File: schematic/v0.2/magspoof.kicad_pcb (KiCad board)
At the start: 2 copper layers, 29.2 x 39.4 mm, 23 parts, among them IC1 STM32F042G6U6, IC3 DRV8835DSSR, P1 USB_A, P2 Expansion Port, P3 Ext Clock, P4 Program Port, SW1 Select, SW2 FIRE!, U1 MCP73831-2-OT

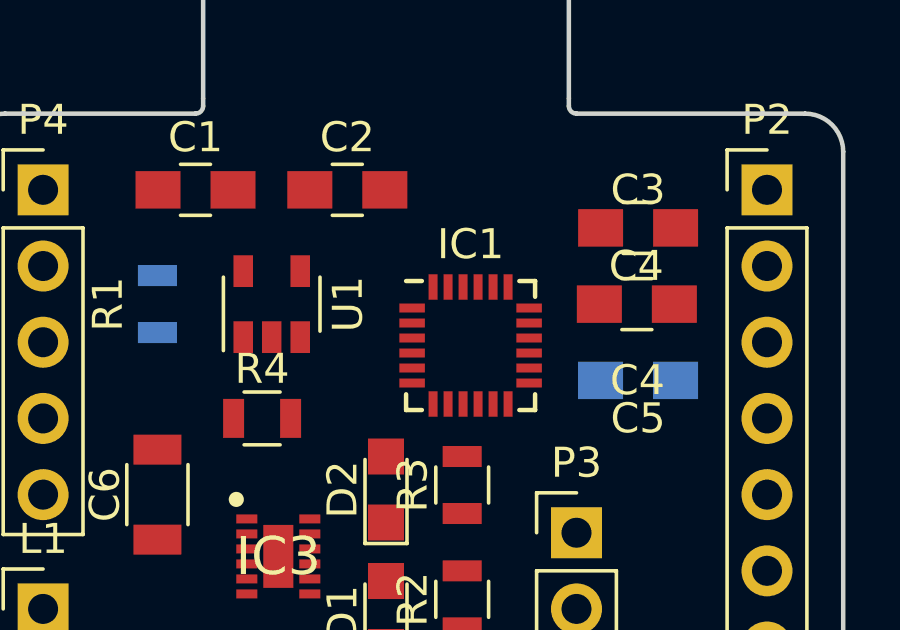
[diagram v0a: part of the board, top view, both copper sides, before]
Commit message: Changed stm32 footprint
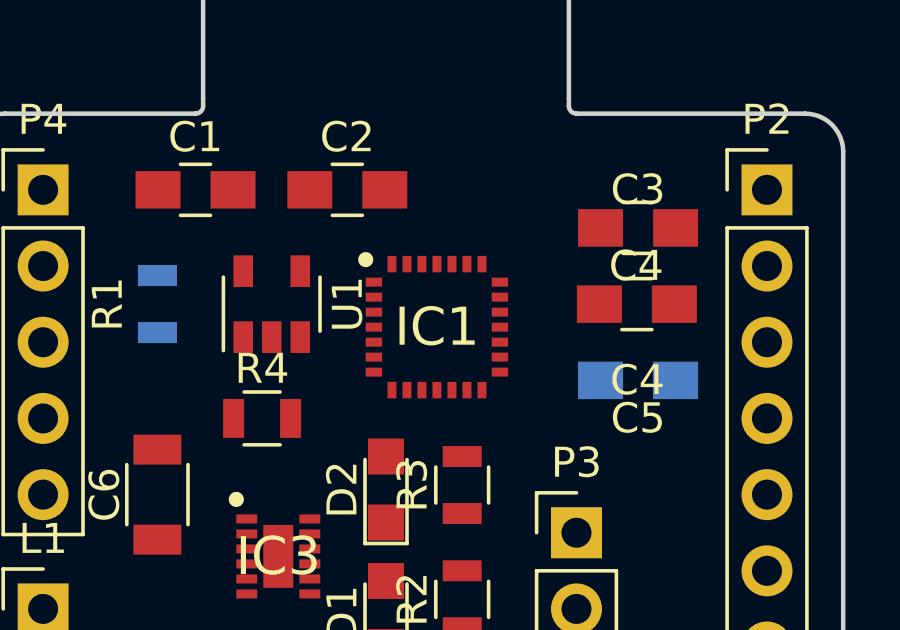
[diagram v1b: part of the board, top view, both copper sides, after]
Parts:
- IC1: footprint Housings_DFN_QFN:QFN-24_4x4mm_Pitch0.5mm -> STM32F042G6U6:QFN50P400X400X60-28N
- moved IC1 1.28 mm to (151.6, 104.9)
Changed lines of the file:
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@@
 (kicad_pcb (version 4) (host pcbnew 4.0.4-stable)
   (general
-    (links 51)
-    (no_connects 51)
-    (area 0 0 0 0)
+    (links 55)
+    (no_connects 55)
+    (area 135.814999 85.014999 165.175001 124.535001)
     (thickness 1.6)
     (drawings 16)
@@
     )
   )
-  (module Housings_DFN_QFN:QFN-24_4x4mm_Pitch0.5mm (layer F.Cu)
-    (at 152.68 105.52)
-    (descr "24-Lead Plastic Quad Flat, No Lead Package (MJ) - 4x4x0.9 mm Body [QFN]; (see Microchip Packaging Specification 00000049BS.pdf)")
-    (tags "QFN 0.5")
-    (attr smd)
-    (fp_text reference IC1 (at 0 -3.375) (layer F.SilkS)
-      (effects (font (size 1 1) (thickness 0.15)))
-    )
-    (fp_text value STM32F042G6U6 (at 0 3.375) (layer F.Fab)
-      (effects (font (size 1 1) (thickness 0.15)))
-    )
-    (fp_line (start -1 -2) (end 2 -2) (layer F.Fab) (width 0.15))
-    (fp_line (start 2 -2) (end 2 2) (layer F.Fab) (width 0.15))
-    (fp_line (start 2 2) (end -2 2) (layer F.Fab) (width 0.15))
-    (fp_line (start -2 2) (end -2 -1) (layer F.Fab) (width 0.15))
-    (fp_line (start -2 -1) (end -1 -2) (layer F.Fab) (width 0.15))
-    (fp_line (start -2.65 -2.65) (end -2.65 2.65) (layer F.CrtYd) (width 0.05))
-    (fp_line (start 2.65 -2.65) (end 2.65 2.65) (layer F.CrtYd) (width 0.05))
-    (fp_line (start -2.65 -2.65) (end 2.65 -2.65) (layer F.CrtYd) (width 0.05))
-    (fp_line (start -2.65 2.65) (end 2.65 2.65) (layer F.CrtYd) (width 0.05))
-    (fp_line (start 2.15 -2.15) (end 2.15 -1.625) (layer F.SilkS) (width 0.15))
-    (fp_line (start -2.15 2.15) (end -2.15 1.625) (layer F.SilkS) (width 0.15))
-    (fp_line (start 2.15 2.15) (end 2.15 1.625) (layer F.SilkS) (width 0.15))
-    (fp_line (start -2.15 -2.15) (end -1.625 -2.15) (layer F.SilkS) (width 0.15))
-    (fp_line (start -2.15 2.15) (end -1.625 2.15) (layer F.SilkS) (width 0.15))
-    (fp_line (start 2.15 2.15) (end 1.625 2.15) (layer F.SilkS) (width 0.15))
-    (fp_line (start 2.15 -2.15) (end 1.625 -2.15) (layer F.SilkS) (width 0.15))
-    (pad 1 smd rect (at -1.95 -1.25) (size 0.85 0.3) (layers F.Cu F.Paste F.Mask)
-      (net 8 "Net-(IC1-Pad1)"))
-    (pad 2 smd rect (at -1.95 -0.75) (size 0.85 0.3) (layers F.Cu F.Paste F.Mask)
-      (net 9 "Net-(IC1-Pad2)"))
-    (pad 3 smd rect (at -1.95 -0.25) (size 0.85 0.3) (layers F.Cu F.Paste F.Mask)
-      (net 10 "Net-(IC1-Pad3)"))
-    (pad 4 smd rect (at -1.95 0.25) (size 0.85 0.3) (layers F.Cu F.Paste F.Mask)
-      (net 11 RESET))
-    (pad 5 smd rect (at -1.95 0.75) (size 0.85 0.3) (layers F.Cu F.Paste F.Mask)
-      (net 12 "Net-(IC1-Pad5)"))
-    (pad 6 smd rect (at -1.95 1.25) (size 0.85 0.3) (layers F.Cu F.Paste F.Mask)
-      (net 13 "Net-(IC1-Pad6)"))
-    (pad 7 smd rect (at -1.25 1.95 90) (size 0.85 0.3) (layers F.Cu F.Paste F.Mask)
-      (net 14 "Net-(IC1-Pad7)"))
-    (pad 8 smd rect (at -0.75 1.95 90) (size 0.85 0.3) (layers F.Cu F.Paste F.Mask)
-      (net 6 LED1))
-    (pad 9 smd rect (at -0.25 1.95 90) (size 0.85 0.3) (layers F.Cu F.Paste F.Mask)
-      (net 15 "Net-(IC1-Pad9)"))
-    (pad 10 smd rect (at 0.25 1.95 90) (size 0.85 0.3) (layers F.Cu F.Paste F.Mask)
-      (net 16 "Net-(IC1-Pad10)"))
-    (pad 11 smd rect (at 0.75 1.95 90) (size 0.85 0.3) (layers F.Cu F.Paste F.Mask)
-      (net 17 SW2))
-    (pad 12 smd rect (at 1.25 1.95 90) (size 0.85 0.3) (layers F.Cu F.Paste F.Mask)
-      (net 18 SW1))
-    (pad 13 smd rect (at 1.95 1.25) (size 0.85 0.3) (layers F.Cu F.Paste F.Mask)
-      (net 4 LED2))
-    (pad 14 smd rect (at 1.95 0.75) (size 0.85 0.3) (layers F.Cu F.Paste F.Mask)
-      (net 19 STATUS_LED))
-    (pad 15 smd rect (at 1.95 0.25) (size 0.85 0.3) (layers F.Cu F.Paste F.Mask)
-      (net 20 "Net-(IC1-Pad15)"))
-    (pad 16 smd rect (at 1.95 -0.25) (size 0.85 0.3) (layers F.Cu F.Paste F.Mask)
-      (net 2 GND))
-    (pad 17 smd rect (at 1.95 -0.75) (size 0.85 0.3) (layers F.Cu F.Paste F.Mask)
-      (net 1 VCC))
-    (pad 18 smd rect (at 1.95 -1.25) (size 0.85 0.3) (layers F.Cu F.Paste F.Mask)
-      (net 1 VCC))
-    (pad 19 smd rect (at 1.25 -1.95 90) (size 0.85 0.3) (layers F.Cu F.Paste F.Mask)
-      (net 21 USB_DM))
-    (pad 20 smd rect (at 0.75 -1.95 90) (size 0.85 0.3) (layers F.Cu F.Paste F.Mask)
-      (net 22 SWCLK))
-    (pad 21 smd rect (at 0.25 -1.95 90) (size 0.85 0.3) (layers F.Cu F.Paste F.Mask)
-      (net 23 SWDIO))
-    (pad 22 smd rect (at -0.25 -1.95 90) (size 0.85 0.3) (layers F.Cu F.Paste F.Mask)
-      (net 24 "Net-(IC1-Pad22)"))
-    (pad 23 smd rect (at -0.75 -1.95 90) (size 0.85 0.3) (layers F.Cu F.Paste F.Mask)
-      (net 25 "Net-(IC1-Pad23)"))
-    (pad 24 smd rect (at -1.25 -1.95 90) (size 0.85 0.3) (layers F.Cu F.Paste F.Mask)
-      (net 26 "Net-(IC1-Pad24)"))
-    (model ${KISYS3DMOD}/Housings_DFN_QFN.3dshapes/QFN-24-1EP_4x4mm_Pitch0.5mm.wrl
-      (at (xyz 0 0 0))
-      (scale (xyz 1 1 1))
-      (rotate (xyz 0 0 0))
-    )
-  )
   (module DRV8835DSSR:SON50P200X300X80-13N (layer F.Cu)
     (at 146.27 112.55)
@@
     )
   )
+  (module STM32F042G6U6:QFN50P400X400X60-28N (layer F.Cu)
+    (at 151.5585 104.9065)
+    (descr UFQFPN28)
+    (tags "Integrated Circuit")
+    (attr smd)
+    (fp_text reference IC1 (at 0 0) (layer F.SilkS)
+      (effects (font (size 1.27 1.27) (thickness 0.254)))
+    )
+    (fp_text value STM32F042G6U6 (at 0 0) (layer F.SilkS) hide
+      (effects (font (size 1.27 1.27) (thickness 0.254)))
+    )
+    (fp_line (start -2.625 -2.625) (end 2.625 -2.625) (layer Dwgs.User) (width 0.05))
+    (fp_line (start 2.625 -2.625) (end 2.625 2.625) (layer Dwgs.User) (width 0.05))
+    (fp_line (start 2.625 2.625) (end -2.625 2.625) (layer Dwgs.User) (width 0.05))
+    (fp_line (start -2.625 2.625) (end -2.625 -2.625) (layer Dwgs.User) (width 0.05))
+    (fp_line (start -2 -2) (end 2 -2) (layer Dwgs.User) (width 0.1))
+    (fp_line (start 2 -2) (end 2 2) (layer Dwgs.User) (width 0.1))
+    (fp_line (start 2 2) (end -2 2) (layer Dwgs.User) (width 0.1))
+    (fp_line (start -2 2) (end -2 -2) (layer Dwgs.User) (width 0.1))
+    (fp_line (start -2 -1.5) (end -1.5 -2) (layer Dwgs.User) (width 0.1))
+    (fp_circle (center -2.375 -2.25) (end -2.25 -2.25) (layer F.SilkS) (width 0.254))
+    (pad 1 smd rect (at -2.1 -1.5 90) (size 0.3 0.55) (layers F.Cu F.Paste F.Mask)
+      (net 8 "Net-(IC1-Pad1)"))
+    (pad 2 smd rect (at -2.1 -1 90) (size 0.3 0.55) (layers F.Cu F.Paste F.Mask)
+      (net 9 "Net-(IC1-Pad2)"))
+    (pad 3 smd rect (at -2.1 -0.5 90) (size 0.3 0.55) (layers F.Cu F.Paste F.Mask)
+      (net 10 "Net-(IC1-Pad3)"))
+    (pad 4 smd rect (at -2.1 0 90) (size 0.3 0.55) (layers F.Cu F.Paste F.Mask)
+      (net 11 RESET))
+    (pad 5 smd rect (at -2.1 0.5 90) (size 0.3 0.55) (layers F.Cu F.Paste F.Mask)
+      (net 12 "Net-(IC1-Pad5)"))
+    (pad 6 smd rect (at -2.1 1 90) (size 0.3 0.55) (layers F.Cu F.Paste F.Mask)
+      (net 13 "Net-(IC1-Pad6)"))
+    (pad 7 smd rect (at -2.1 1.5 90) (size 0.3 0.55) (layers F.Cu F.Paste F.Mask)
+      (net 14 "Net-(IC1-Pad7)"))
+    (pad 8 smd rect (at -1.5 2.1) (size 0.3 0.55) (layers F.Cu F.Paste F.Mask)
+      (net 6 LED1))
+    (pad 9 smd rect (at -1 2.1) (size 0.3 0.55) (layers F.Cu F.Paste F.Mask)
+      (net 15 "Net-(IC1-Pad9)"))
+    (pad 10 smd rect (at -0.5 2.1) (size 0.3 0.55) (layers F.Cu F.Paste F.Mask)
+      (net 16 "Net-(IC1-Pad10)"))
+    (pad 11 smd rect (at 0 2.1) (size 0.3 0.55) (layers F.Cu F.Paste F.Mask)
+      (net 17 SW2))
+    (pad 12 smd rect (at 0.5 2.1) (size 0.3 0.55) (layers F.Cu F.Paste F.Mask)
+      (net 18 SW1))
+    (pad 13 smd rect (at 1 2.1) (size 0.3 0.55) (layers F.Cu F.Paste F.Mask)
+      (net 4 LED2))
+    (pad 14 smd rect (at 1.5 2.1) (size 0.3 0.55) (layers F.Cu F.Paste F.Mask)
+      (net 19 STATUS_LED))
+    (pad 15 smd rect (at 2.1 1.5 90) (size 0.3 0.55) (layers F.Cu F.Paste F.Mask)
+      (net 20 "Net-(IC1-Pad15)"))
+    (pad 16 smd rect (at 2.1 1 90) (size 0.3 0.55) (layers F.Cu F.Paste F.Mask)
+      (net 2 GND))
+    (pad 17 smd rect (at 2.1 0.5 90) (size 0.3 0.55) (layers F.Cu F.Paste F.Mask)
+      (net 1 VCC))
+    (pad 18 smd rect (at 2.1 0 90) (size 0.3 0.55) (layers F.Cu F.Paste F.Mask)
+      (net 1 VCC))
+    (pad 19 smd rect (at 2.1 -0.5 90) (size 0.3 0.55) (layers F.Cu F.Paste F.Mask)
+      (net 21 USB_DM))
+    (pad 20 smd rect (at 2.1 -1 90) (size 0.3 0.55) (layers F.Cu F.Paste F.Mask)
+      (net 22 SWCLK))
+    (pad 21 smd rect (at 2.1 -1.5 90) (size 0.3 0.55) (layers F.Cu F.Paste F.Mask)
+      (net 23 SWDIO))
+    (pad 22 smd rect (at 1.5 -2.1) (size 0.3 0.55) (layers F.Cu F.Paste F.Mask)
+      (net 24 "Net-(IC1-Pad22)"))
+    (pad 23 smd rect (at 1 -2.1) (size 0.3 0.55) (layers F.Cu F.Paste F.Mask)
+      (net 25 "Net-(IC1-Pad23)"))
+    (pad 24 smd rect (at 0.5 -2.1) (size 0.3 0.55) (layers F.Cu F.Paste F.Mask)
+      (net 26 "Net-(IC1-Pad24)"))
+    (pad 25 smd rect (at 0 -2.1) (size 0.3 0.55) (layers F.Cu F.Paste F.Mask)
+      (net 33 "Net-(IC1-Pad25)"))
+    (pad 26 smd rect (at -0.5 -2.1) (size 0.3 0.55) (layers F.Cu F.Paste F.Mask)
+      (net 34 "Net-(IC1-Pad26)"))
+    (pad 27 smd rect (at -1 -2.1) (size 0.3 0.55) (layers F.Cu F.Paste F.Mask)
+      (net 35 "Net-(IC1-Pad27)"))
+    (pad 28 smd rect (at -1.5 -2.1) (size 0.3 0.55) (layers F.Cu F.Paste F.Mask)
+      (net 36 "Net-(IC1-Pad28)"))
+  )
   (gr_line (start 155.956 97.536) (end 155.956 97.282) (layer Edge.Cuts) (width 0.15))

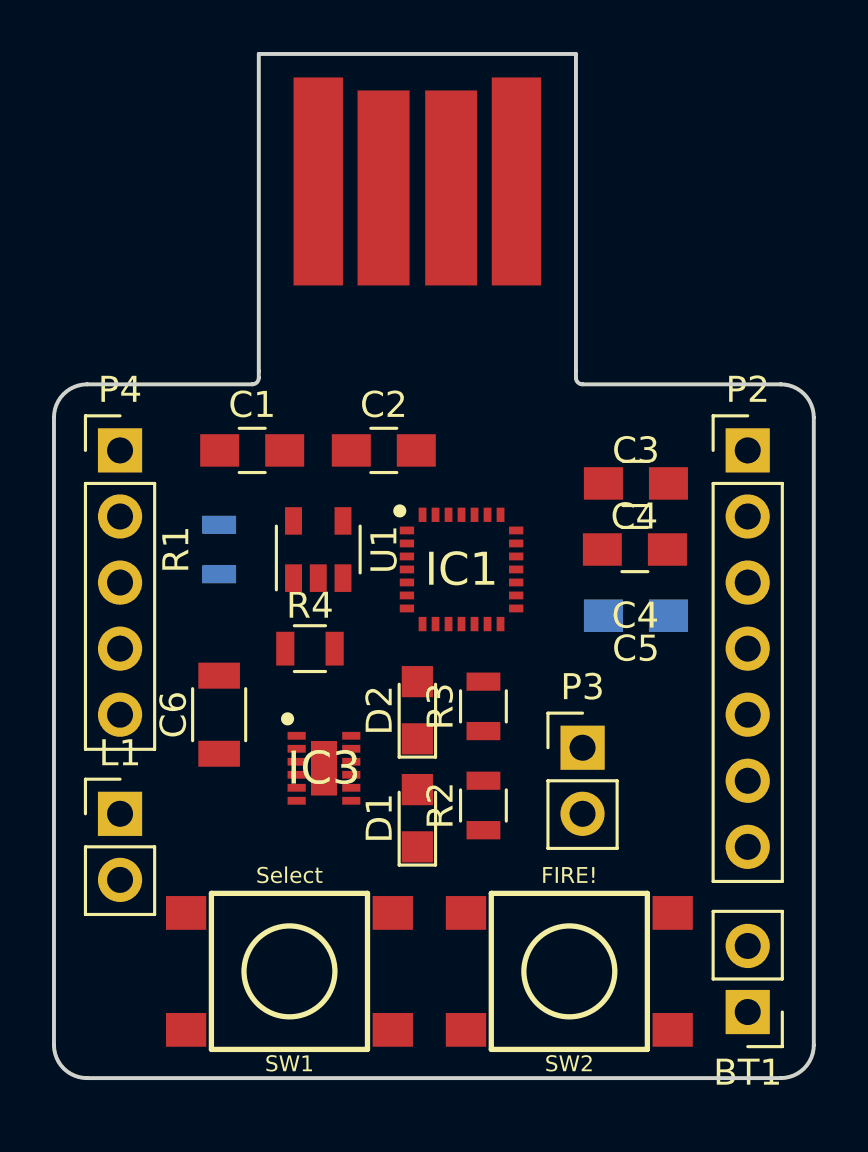
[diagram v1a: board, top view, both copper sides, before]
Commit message: Completed traces on v2
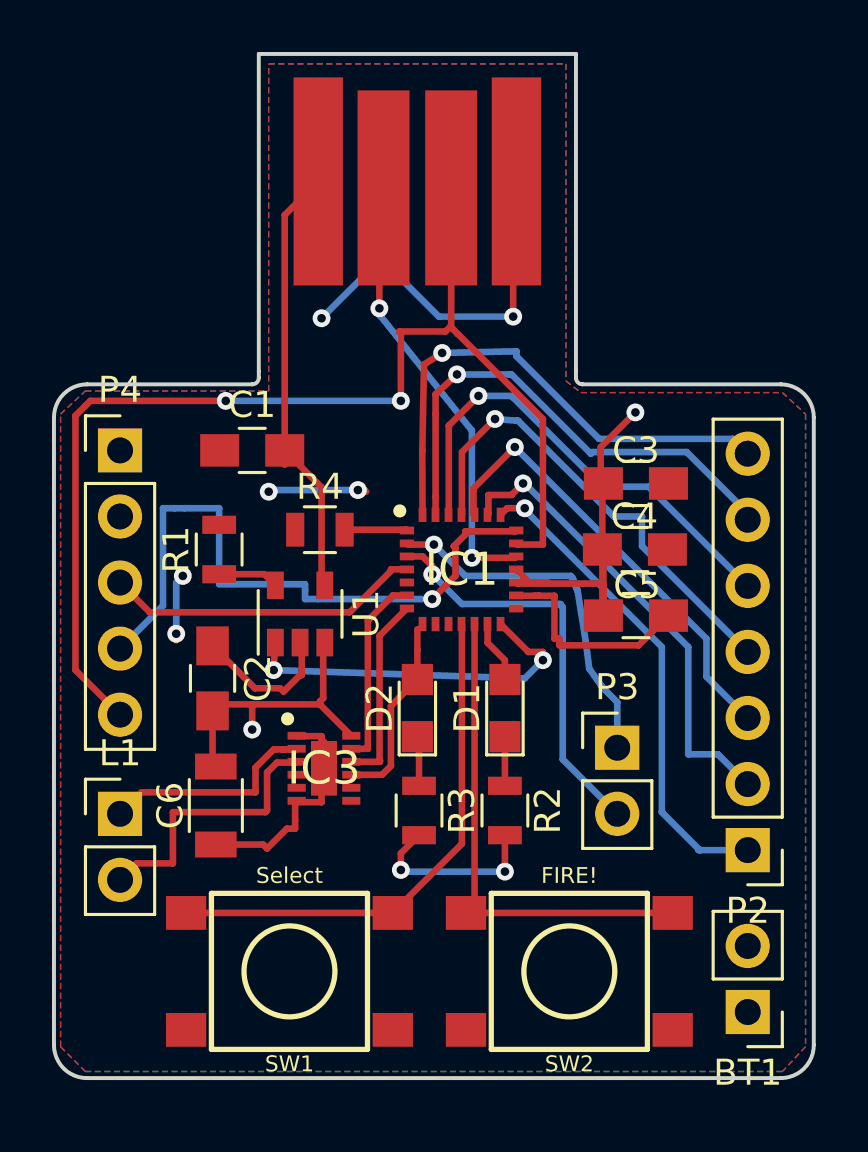
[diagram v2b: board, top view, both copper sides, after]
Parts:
- C5, R1: moved to F.Cu
- moved P2 15.4 mm to (162.6, 115.7), turned to 180 degrees
- moved C2 11.0 mm to (142.0, 109.1), turned to 270 degrees
- moved D1 5.41 mm to (153.2, 110.2)
- moved R3 4.71 mm to (149.9, 114.2), turned to 270 degrees
- moved R4 4.59 mm to (146.1, 103.4)
- moved C6 3.49 mm to (142.1, 114.0)
- moved U1 2.57 mm to (145.4, 106.6)
- moved P3 1.33 mm to (157.5, 111.8)
- moved R2 0.85 mm to (153.2, 114.2), turned to 270 degrees
- moved D2 0.08 mm to (149.9, 110.2)
- turned C5 to 0 degrees
- turned R1 to 90 degrees
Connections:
- SW1 pad A1: (no net) -> SW2
- SW1 pad A2: (no net) -> SW2
- SW1 pad B1: (no net) -> GND
- SW1 pad B2: (no net) -> GND
- SW2 pad A1: (no net) -> SW1
- SW2 pad A2: (no net) -> SW1
- SW2 pad B1: (no net) -> GND
- SW2 pad B2: (no net) -> GND
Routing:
- net GND: track 0.00 -> 52.3 mm, vias 0 -> 8
- net SWCLK: track 0.00 -> 46.0 mm, vias 0 -> 2
- net VCC: track 0.00 -> 29.8 mm, vias 0 -> 2
- net SWDIO: track 0.00 -> 25.1 mm, vias 0 -> 1
- net SW2: track 0.00 -> 20.2 mm
- net Net-(IC1-Pad28): track 0.00 -> 20.1 mm, vias 0 -> 1
- net Net-(IC1-Pad27): track 0.00 -> 19.5 mm, vias 0 -> 1
- net SW1: track 0.00 -> 19.2 mm
- net Net-(IC1-Pad22): track 0.00 -> 18.9 mm, vias 0 -> 1
- net Net-(IC1-Pad26): track 0.00 -> 18.5 mm, vias 0 -> 1
- net USB_DM: track 0.00 -> 18.4 mm, vias 0 -> 2
- net Net-(IC1-Pad25): track 0.00 -> 18.3 mm, vias 0 -> 1
- net Net-(IC1-Pad23): track 0.00 -> 18.2 mm, vias 0 -> 1
- net Net-(IC1-Pad24): track 0.00 -> 17.4 mm, vias 0 -> 1
- net USB_VCC: track 0.00 -> 17.3 mm
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- added copper zone on F.Cu, net GND
- added copper zone on B.Cu, net VCC
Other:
- net class Default: clearance 0.2 -> 0.1524; trace_width 0.25 -> 0.254; via_dia 0.6 -> 0.6858; via_drill 0.4 -> 0.3302
- rule trace_clearance: 0.2 -> 0.1524
- rule trace_min: 0.2 -> 0.1524
- rule via_min_drill: 0.3 -> 0.3302
- rule via_min_size: 0.4 -> 0.6858

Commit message: Completed traces on v2 --trying to make things neater without destroying everything
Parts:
- added REF***: OSHW-Logo_5.7x6mm_SilkScreen, Symbols:OSHW-Logo_5.7x6mm_SilkScreen, B.Cu at (140.1, 120.7)
- renumbered SW1 to FIRE!, SW2 to Select
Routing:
- net GND: track 52.3 -> 49.6 mm
- net USB_DM: track 18.4 -> 19.5 mm
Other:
- board text added: "+"
- board text added: "-"
- board text added: "RickMagSpoof v2"
- board text added: "WR"
